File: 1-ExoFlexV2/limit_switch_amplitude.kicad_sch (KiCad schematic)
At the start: 29 parts, among them J90 Jumper, J91 Jumper, J92 Jumper, U11 Inverter, U42 Inverter, U43 Inverter, U49 OR GATE 3IN

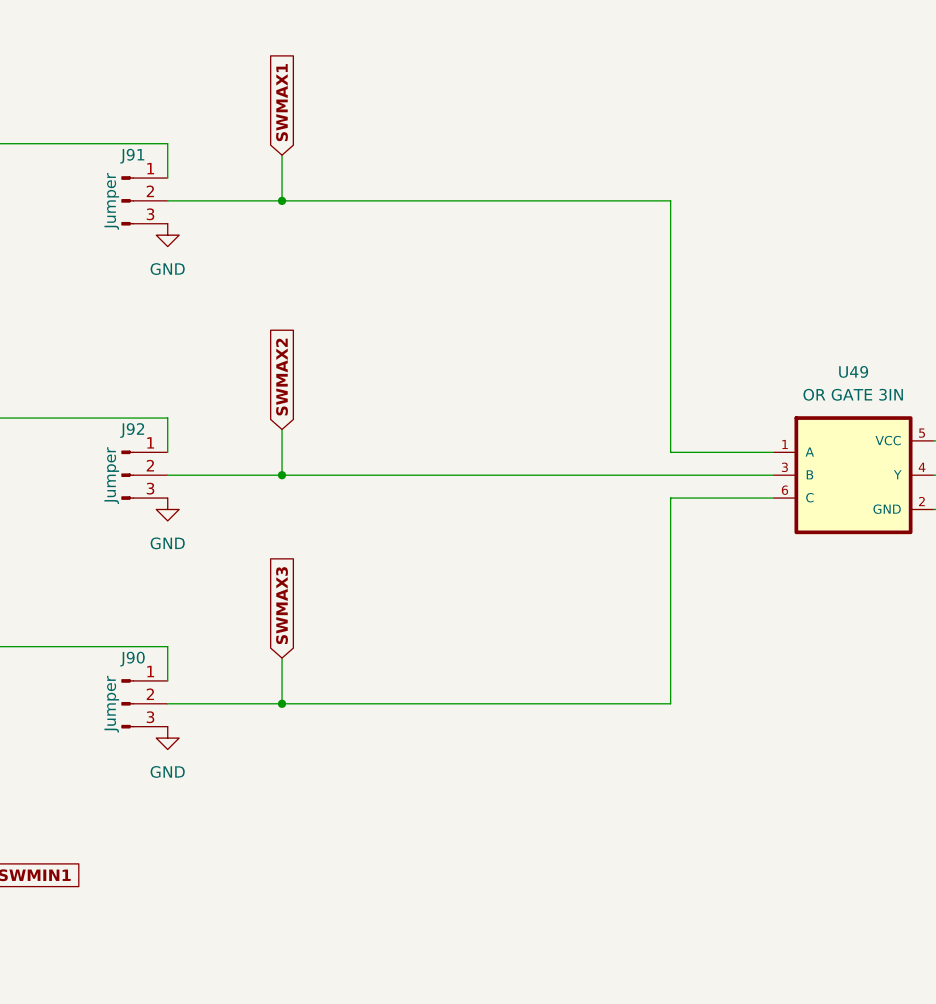
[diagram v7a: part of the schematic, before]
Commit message: Routage pour Review 1
- Replacement des test point pour faciliter le rework
- Correction des erreurs dans le BOM
-
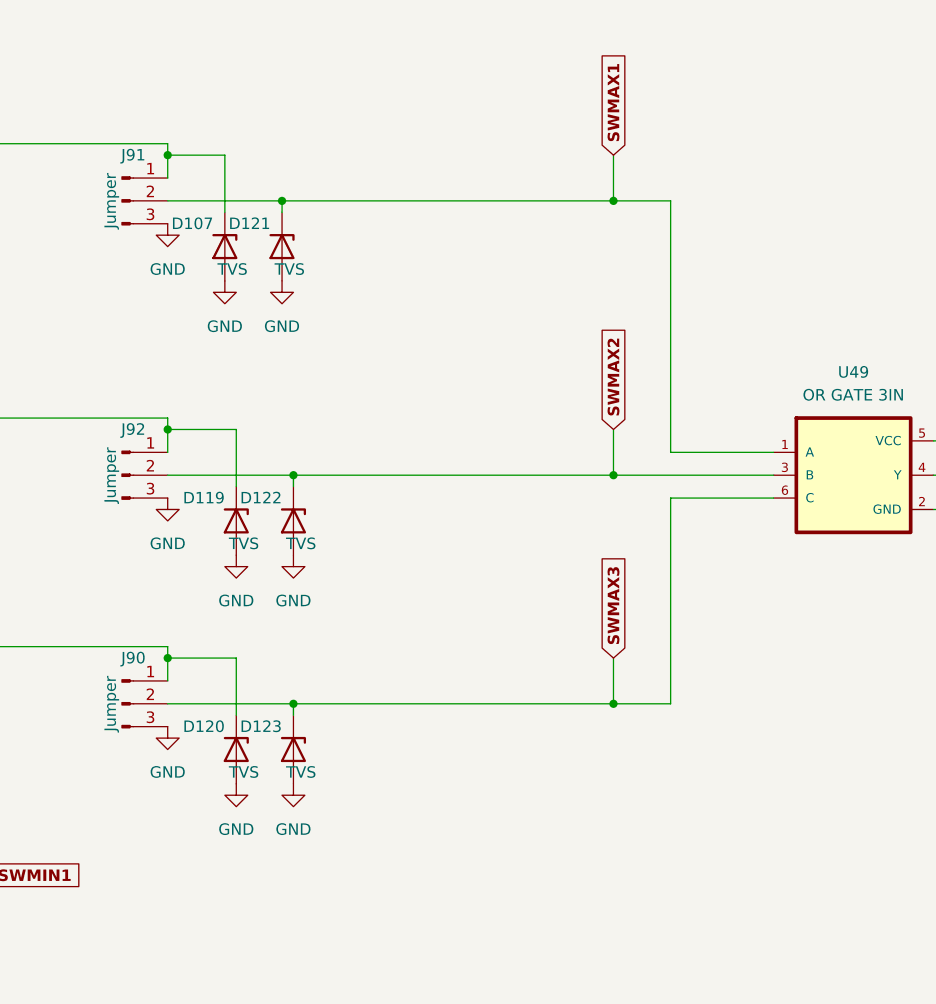
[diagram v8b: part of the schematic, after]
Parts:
- added D107, D119, D120, D121, D122, D123: TVS, FootPrint:DPY2_TEX, symbol Device:D_Zener
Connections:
- net GND: now also D107.2 (A), D119.2 (A), D120.2 (A), D121.2 (A), D122.2 (A), D123.2 (A)
- net SWMAX1: now also D121.1 (K)
- net SWMAX2: now also D122.1 (K)
- net SWMAX3: now also D123.1 (K)
- net at J92.1 (Pin_1), U11.5 (2Y): now also D119.1 (K)
- net at J90.1 (Pin_1), U11.2 (3Y): now also D120.1 (K)
- net at J91.1 (Pin_1), U11.7 (1Y): now also D107.1 (K)
